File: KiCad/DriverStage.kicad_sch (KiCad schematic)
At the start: 21 parts, among them CN201 MR60-F, U201 DRV8323HRTAT

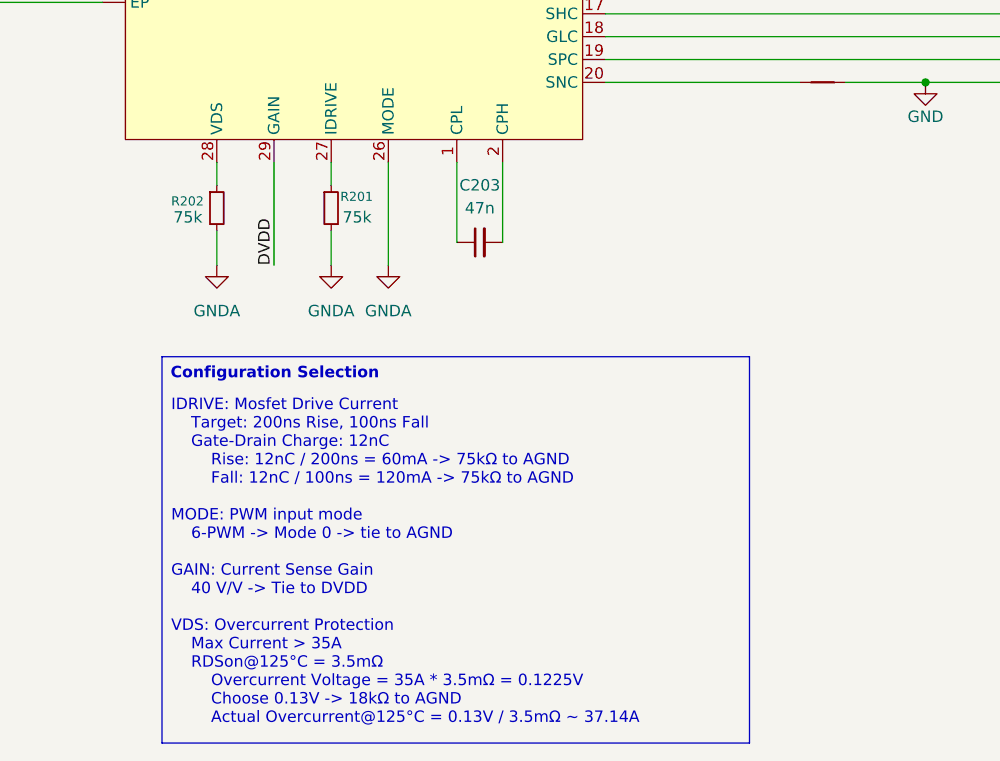
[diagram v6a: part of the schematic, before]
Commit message: updated configuration for new mosfets
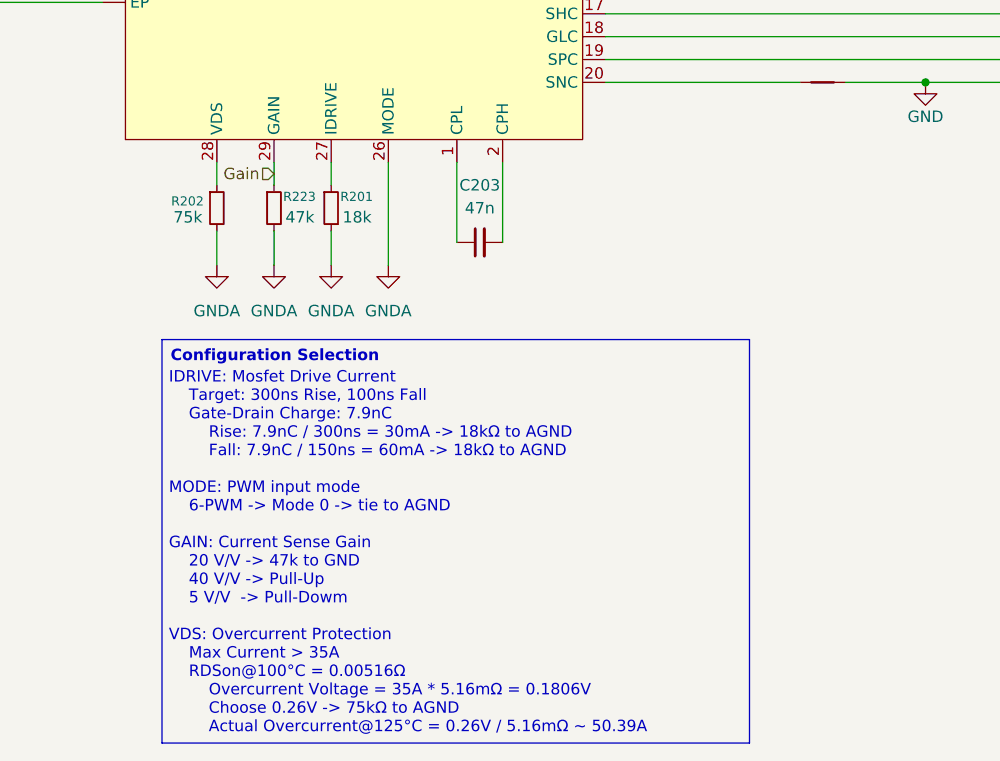
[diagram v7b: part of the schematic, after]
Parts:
- added R223: 47k, Resistor_SMD:R_0402_1005Metric, symbol Device:R_Small
- R201: value 75k -> 18k
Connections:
- net DVDD: no longer U201.29 (GAIN)
- net GND: now also R223.2
- new net Gain: R223.1, U201.29 (GAIN)
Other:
- note added: "IDRIVE: Mosfet Drive Current Target: 300ns Rise, 100ns Fall Gate-Drain Charge: 7.9nC Rise: 7.9nC / 300ns = 30mA -> 18kΩ to AGND Fall: 7.9nC / 150ns = 60mA -> 18kΩ to AGND MODE: PWM input mode 6-PWM -> Mode 0 -> tie to AGND GAIN: Current Sense Gain 20 V/V -> 47k to GND 40 V/V -> Pull-Up 5 V/V -> Pull-Dowm VDS: Overcurrent Protection Max Current > 35A RDSon@100°C = 0.00516Ω Overcurrent Voltage = 35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"
- note removed: "IDRIVE: Mosfet Drive Current Target: 200ns Rise, 100ns Fall Gate-Drain Charge: 12nC Rise: 12nC / 200ns = 60mA -> 75kΩ to AGND Fall: 12nC / 100ns = 120mA -> 75kΩ to AGND MODE: PWM input mode 6-PWM -> Mode 0 -> tie to AGND GAIN: Current Sense Gain 40 V/V -> Tie to DVDD VDS: Overcurrent Protection Max Current > 35A RDSon@125°C = 3.5mΩ Overcurrent Voltage = 35A * 3.5mΩ = 0.1225V Choose 0.13V -> 18kΩ 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"
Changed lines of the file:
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@@
 	(generator_version "10.0")
 	(paper "A4")
-	(text "IDRIVE: Mosfet Drive Current\n	Target: 200ns Rise, 100ns Fall\n	Gate-Drain Charge: 12nC\n		Rise: 12nC / 200ns = 60mA -> 75kΩ to AGND\n		Fall: 12nC / 100ns = 120mA -> 75kΩ to AGND\n\nMODE: PWM input mode\n	6-PWM -> Mode 0 -> tie to AGND\n\nGAIN: Current Sense Gain\n	40 V/V -> Tie to DVDD\n\nVDS: Overcurrent Protection\n	Max Current > 35A\n	RDSon@125°C = 3.5mΩ\n		Overcurrent Voltage = 35A * 3.5mΩ = 0.1225V\n		Choose 0.13V -> 18kΩ to AGND\n		Actual Overcurrent@125°C = 0.13V / 3.5mΩ ~ 37.14A"
+	(text "IDRIVE: Mosfet Drive Current\n	Target: 300ns Rise, 100ns Fall\n	Gate-Drain Charge: 7.9nC\n		Rise: 7.9nC / 300ns = 30mA -> 18kΩ to AGND\n		Fall: 7.9nC / 150ns = 60mA -> 18kΩ to AGND\n\nMODE: PWM input mode\n	6-PWM -> Mode 0 -> tie to AGND\n\nGAIN: Current Sense Gain\n	20 V/V -> 47k to GND\n	40 V/V -> Pull-Up\n	5 V/V  -> Pull-Dowm\n\nVDS: Overcurrent Protection\n	Max Current > 35A\n	RDSon@100°C = 0.00516Ω\n		Overcurrent Voltage = 35A * 5.16mΩ = 0.1806V\n		Choose 0.26V -> 75kΩ to AGND\n		Actual Overcurrent@125°C = 0.26V / 5.16mΩ ~ 50.39A"
 		(exclude_from_sim no)
-		(at 67.31 176.53 0)
+		(at 67.056 175.514 0)
 		(effects
 			(font
@@
 	(text_box "Configuration Selection"
 		(exclude_from_sim no)
-		(at 66.294 153.67 0)
-		(size 65.278 42.926)
+		(at 66.294 151.765 0)
+		(size 65.278 44.831)
 		(margins 0.9525 0.9525 0.9525 0.9525)
 		(stroke
@@
 	(wire
 		(pts
-			(xy 78.74 132.08) (xy 78.74 143.51)
-		)
-		(stroke
-			(width 0)
-			(type default)
-		)
-	)
-	(wire
-		(pts
 			(xy 38.1 54.61) (xy 50.8 54.61)
 		)
@@
 	(wire
 		(pts
+			(xy 78.74 139.7) (xy 78.74 143.51)
+		)
+		(stroke
+			(width 0)
+			(type default)
+		)
+	)
+	(wire
+		(pts
 			(xy 271.78 53.34) (xy 275.59 53.34)
 		)
@@
 	(wire
 		(pts
+			(xy 78.74 132.08) (xy 78.74 134.62)
+		)
+		(stroke
+			(width 0)
+			(type default)
+		)
+	)
+	(wire
+		(pts
 			(xy 54.61 87.63) (xy 59.69 87.63)
 		)
@@
 		)
 	)
-	(label "DVDD"
-		(at 78.74 143.51 90)
-		(effects
-			(font
-				(size 1.27 1.27)
-			)
-			(justify left bottom)
-		)
-	)
 	(hierarchical_label "SOA"
 		(shape output)
@@
 		)
 	)
+	(hierarchical_label "Gain"
+		(shape input)
+		(at 78.74 133.35 180)
+		(effects
+			(font
+				(size 1.27 1.27)
+			)
+			(justify right)
+		)
+	)
 	(hierarchical_label "INLB"
 		(shape input)
@@
 	(symbol
 		(lib_id "power:GNDA")
+		(at 78.74 143.51 0)
+		(unit 1)
+		(body_style 1)
+		(exclude_from_sim no)
+		(in_bom yes)
+		(on_board yes)
+		(in_pos_files yes)
+		(dnp no)
+		(fields_autoplaced yes)
+		(property "Reference" "#PWR0223"
+			(at 78.74 149.86 0)
+			(hide yes)
+			(show_name no)
+			(do_not_autoplace no)
+			(effects
+				(font
+					(size 1.27 1.27)
+				)
+			)
+		)
+		(property "Value" "GNDA"
+			(at 78.74 148.59 0)
+			(show_name no)
+			(do_not_autoplace no)
+			(effects
+				(font
+					(size 1.27 1.27)
+				)
+			)
+		)
+		(property "Footprint" ""
+			(at 78.74 143.51 0)
+			(hide yes)
+			(show_name no)
+			(do_not_autoplace no)
+			(effects
+				(font
+					(size 1.27 1.27)
+				)
+			)
+		)
+		(property "Datasheet" ""
+			(at 78.74 143.51 0)
+			(hide yes)
+			(show_name no)
+			(do_not_autoplace no)
+			(effects
+				(font
+					(size 1.27 1.27)
+				)
+			)
+		)
+		(property "Description" "Power symbol creates a global label with name \"GNDA\" , analog ground"
+			(at 78.74 143.51 0)
+			(hide yes)
+			(show_name no)
+			(do_not_autoplace no)
+			(effects
+				(font
+					(size 1.27 1.27)
+				)
+			)
+		)
+		(pin "1"
+		)
+		(instances
+			(project "simpleFOC Dual Motor Controller"
+				(path "/0dffc378-5905-459a-b0cb-e8e514a8bbef/de390f81-41fc-4236-a904-44260774a171"
+					(reference "#PWR0223")
+					(unit 1)
+				)
+				(path "/0dffc378-5905-459a-b0cb-e8e514a8bbef/f2c2b770-272c-4740-ba73-c3bb2a232079"
+					(reference "#PWR0601")
+					(unit 1)
+				)
+			)
+		)
+	)
+	(symbol
+		(lib_id "power:GNDA")
 		(at 44.45 134.62 0)
 		(unit 1)
@@
 			)
 		)
-		(property "Value" "75k"
+		(property "Value" "18k"
 			(at 86.36 138.176 0)
 			(show_name no)
@@
 					(unit 1)
 				)
+			)
+		)
+	)
+	(symbol
+		(lib_id "Device:R_Small")
+		(at 78.74 137.16 0)
+		(unit 1)
+		(body_style 1)
+		(exclude_from_sim no)
+		(in_bom yes)
+		(on_board yes)
+		(in_pos_files yes)
+		(dnp no)
+		(property "Reference" "R223"
+			(at 79.756 135.89 0)
+			(show_name no)
+			(do_not_autoplace no)
+			(effects
+				(font
+					(size 1.016 1.016)
+				)
+				(justify left)
+			)
+		)
+		(property "Value" "47k"
+			(at 80.01 138.176 0)
+			(show_name no)
+			(do_not_autoplace no)
+			(effects
+				(font
+					(size 1.27 1.27)
+				)
+				(justify left)
+			)
+		)
+		(property "Footprint" "Resistor_SMD:R_0402_1005Metric"
+			(at 78.74 137.16 0)
+			(hide yes)
+			(show_name no)
+			(do_not_autoplace no)
+			(effects
+				(font
+					(size 1.27 1.27)
+				)
+			)
+		)
+		(property "Datasheet" ""
+			(at 78.74 137.16 0)
+			(hide yes)
+			(show_name no)
+			(do_not_autoplace no)
+			(effects
+				(font
+					(size 1.27 1.27)
+				)
+			)
+		)
+		(property "Description" "Resistor, small symbol"
+			(at 78.74 137.16 0)
+			(hide yes)
+			(show_name no)
+			(do_not_autoplace no)
+			(effects
+				(font
+					(size 1.27 1.27)
+				)
+			)
+		)
+		(pin "1"
+		)
+		(pin "2"
+		)
+		(instances
+			(project "simpleFOC Dual Motor Controller"
+				(path "/0dffc378-5905-459a-b0cb-e8e514a8bbef/de390f81-41fc-4236-a904-44260774a171"
+					(reference "R223")
+					(unit 1)
+				)
+				(path "/0dffc378-5905-459a-b0cb-e8e514a8bbef/f2c2b770-272c-4740-ba73-c3bb2a232079"
+					(reference "R601")
+					(unit 1)
+				)

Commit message: started laying out
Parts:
- removed R207, R208: 100k, Resistor_SMD:R_0402_1005Metric, symbol Device:R_Small
- added R224: 47k, Resistor_SMD:R_0402_1005Metric, symbol Device:R_Small
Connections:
- net INLB is gone; now on net ~{HI-Z}: R206.1, U201.37 (INLB)
- net INLC is gone; now on net ~{HI-Z}: U201.39 (INLC)
- net GND: now also R224.2; no longer U201.26 (MODE)
- net INHB: now also R204.1; no longer R205.1
- net INHC: now also R205.1
- net INLA renamed ~{HI-Z}
- net ~{HI-Z}: no longer R204.1
- new net: R224.1, U201.26 (MODE)
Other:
- note added: "IDRIVE: Mosfet Drive Current Target: 300ns Rise, 100ns Fall Gate-Drain Charge: 7.9nC Rise: 7.9nC / 300ns = 30mA -> 18kΩ to AGND Fall: 7.9nC / 150ns = 60mA -> 18kΩ to AGND MODE: PWM input mode 3-PWM -> Mode 1 -> 47kΩ to AGND GAIN: Current Sense Gain 20 V/V -> 47k to GND 40 V/V -> Pull-Up 5 V/V -> Pull-Dowm VDS: Overcurrent Protection Max Current > 35A RDSon@100°C = 0.00516Ω Overcurrent Voltage = 3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"
- note removed: "IDRIVE: Mosfet Drive Current Target: 300ns Rise, 100ns Fall Gate-Drain Charge: 7.9nC Rise: 7.9nC / 300ns = 30mA -> 18kΩ to AGND Fall: 7.9nC / 150ns = 60mA -> 18kΩ to AGND MODE: PWM input mode 6-PWM -> Mode 0 -> tie to AGND GAIN: Current Sense Gain 20 V/V -> 47k to GND 40 V/V -> Pull-Up 5 V/V -> Pull-Dowm VDS: Overcurrent Protection Max Current > 35A RDSon@100°C = 0.00516Ω Overcurrent Voltage = 35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"
- moved on the sheet: R209, R210
